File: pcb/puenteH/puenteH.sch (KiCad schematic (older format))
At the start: 16 parts

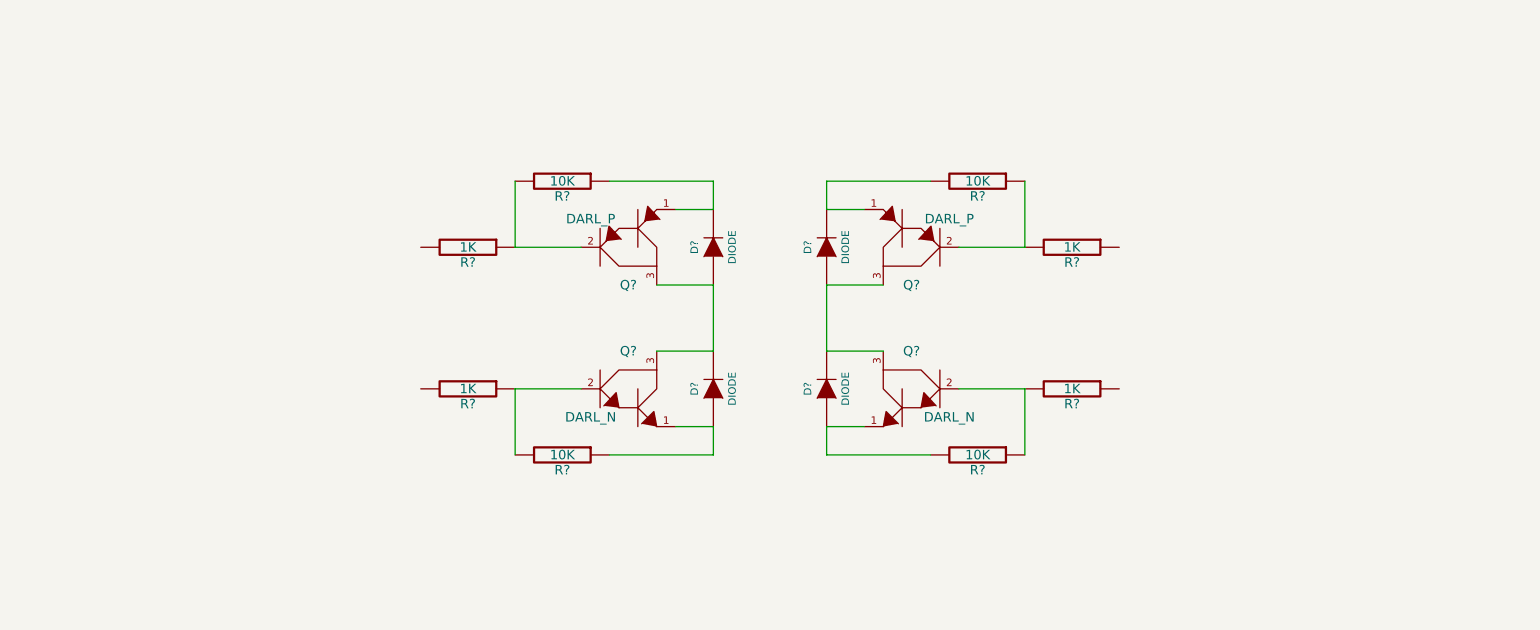
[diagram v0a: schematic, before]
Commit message: Add optos for digital signals
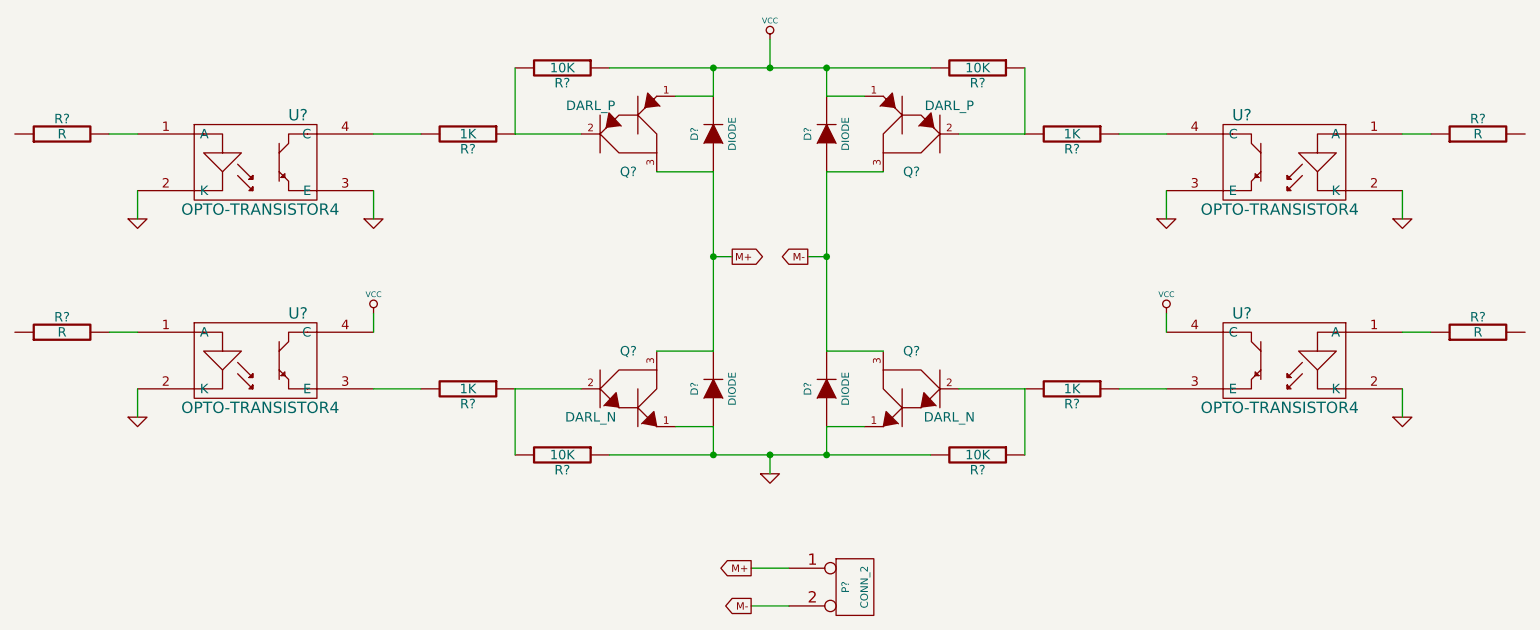
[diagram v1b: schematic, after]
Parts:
- added P?: CONN_2, symbol CONN_2
- added R? (x4): R, symbol R
- added U? (x4): OPTO-TRANSISTOR4, symbol OPTO-TRANSISTOR4
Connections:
- net M+: now reaches D?.1 (A), D?.2 (K), Q?.3, Q?.3
- net M+: now also P?.1 (P1)
- net VCC: now reaches D?.2 (K), Q?.1, R?.1
- net VCC: now also D?.2 (K), Q?.1, R?.2, U?.4 (C), U?.4 (C)
- net M-: now reaches D?.1 (A), D?.2 (K), Q?.3, Q?.3
- net M-: now also P?.2 (PM)
- net GND: now reaches D?.1 (A), Q?.1, R?.2
- net GND: now also D?.1 (A), Q?.1, R?.1, U?.2 (K), U?.2 (K), U?.2 (K), U?.2 (K), U?.3 (E), U?.3 (E)
- net at R?.2: now also U?.3 (E)
- net at R?.2: now also U?.4 (C)
- net at R?.1: now also U?.4 (C)
- net at R?.1: now also U?.3 (E)
- new net: R?.2, U?.1 (A) (x2)
- new net: R?.1, U?.1 (A) (x2)
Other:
- moved on the sheet: D?, Q?, R?

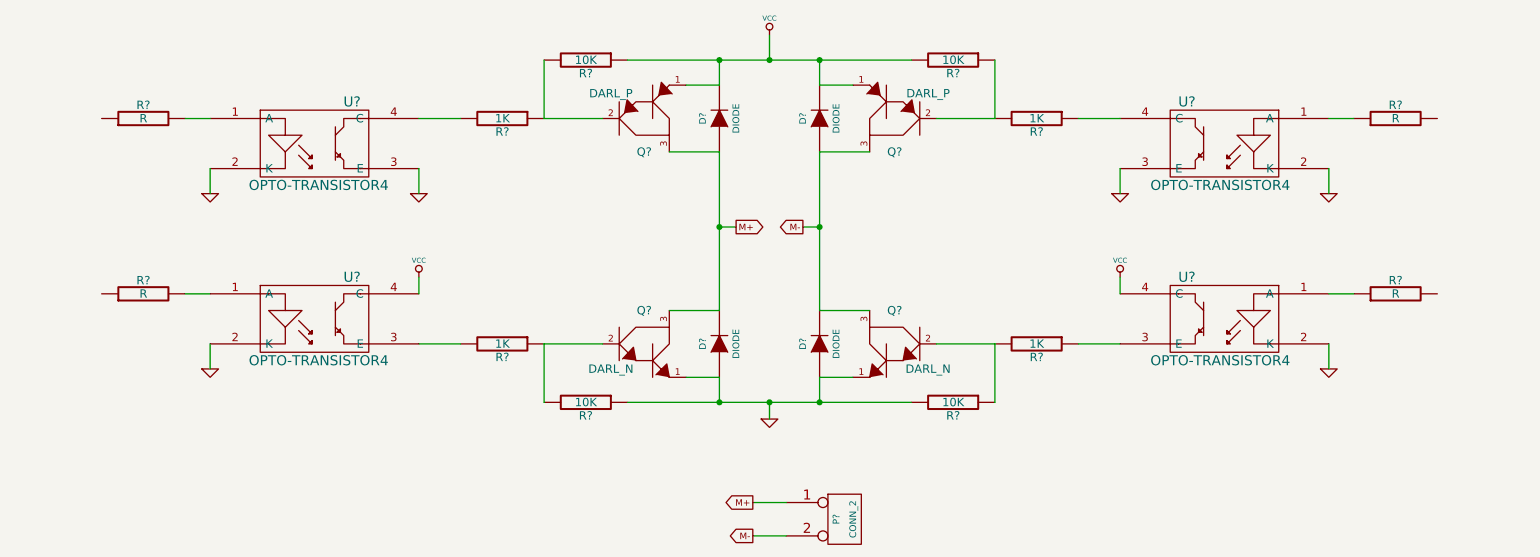
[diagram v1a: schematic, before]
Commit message: Add pins for interface between the H bridge and the uC
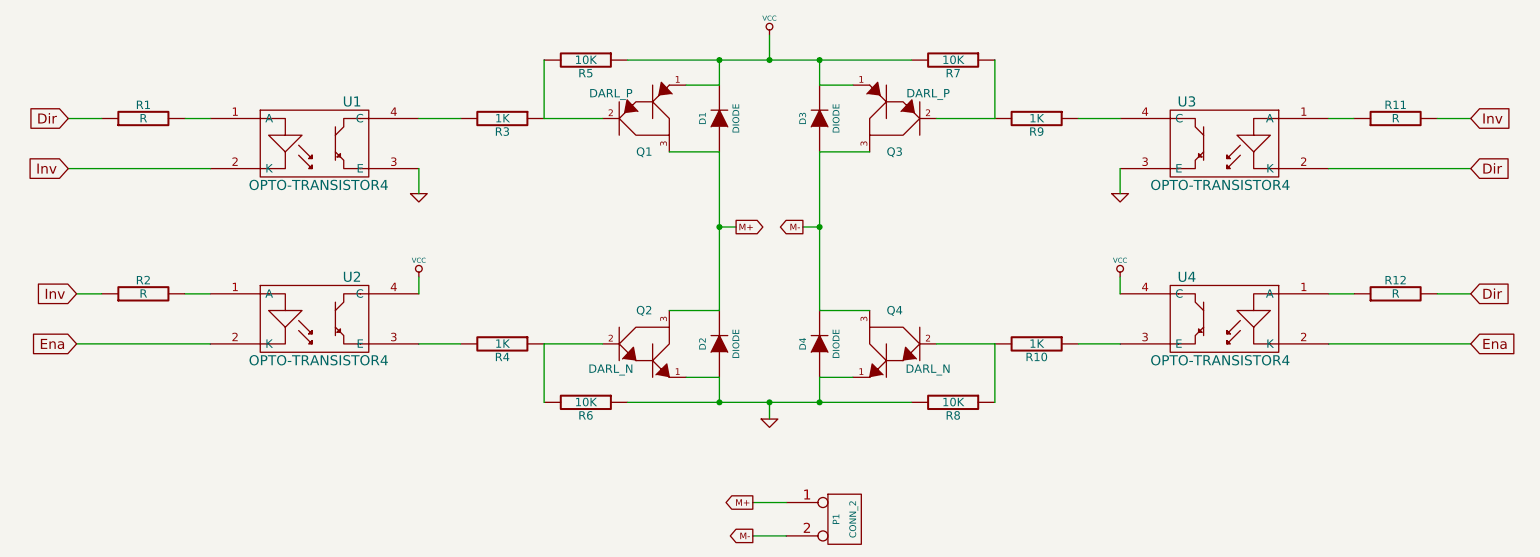
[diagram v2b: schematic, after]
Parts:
- gave numbers to parts that had none: 25
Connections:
- net GND: no longer U1.2 (K), U2.2 (K), U3.2 (K), U4.2 (K)
- net Inv: now reaches R2.1
- net Inv: now also R11.2, U1.2 (K)
- net Dir: now reaches R1.1
- net Dir: now also R12.2, U3.2 (K)
- new net Ena: U2.2 (K), U4.2 (K)
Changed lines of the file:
@@
-EESchema Schematic File Version 2  date mar 11 dic 2012 20:15:30 UYST
+EESchema Schematic File Version 2  date vie 14 dic 2012 20:56:03 UYST
 LIBS:power
 LIBS:device
@@
 Sheet 1 1
 Title "Puente H para motores CC"
-Date "11 dec 2012"
+Date "14 dec 2012"
 Rev "1.0"
 Comp ""
@@
 $EndDescr
 Wire Wire Line
+	9600 3100 9800 3100
+Wire Wire Line
+	1450 4150 1600 4150
+Wire Wire Line
+	9800 4150 9600 4150
+Wire Wire Line
+	1400 3400 2250 3400
+Wire Wire Line
 	7700 4050 7700 4150
 Wire Wire Line
@@
 Wire Wire Line
 	8950 3100 9100 3100
-Wire Wire Line
-	8950 3400 8950 3550
-Wire Wire Line
-	2250 4450 2250 4600
-Wire Wire Line
-	2250 3400 2250 3550
 Wire Wire Line
 	3500 3100 3750 3100
@@
 	2100 4150 2250 4150
 Wire Wire Line
-	8950 4450 8950 4600
-Wire Wire Line
 	8950 4150 9100 4150
 Wire Wire Line
@@
 Wire Wire Line
 	7700 3400 7700 3550
-$Comp
-L VCC #PWR?
+Wire Wire Line
+	1400 3100 1600 3100
+Wire Wire Line
+	2250 4450 1450 4450
+Wire Wire Line
+	9800 4450 8950 4450
+Wire Wire Line
+	8950 3400 9800 3400
+Text GLabel 9800 3400 2    60   Input ~ 0
+Dir
+Text GLabel 1450 4150 0    60   Input ~ 0
+Inv
+Text GLabel 9800 4450 2    60   Input ~ 0
+Ena
+Text GLabel 9800 3100 2    60   Input ~ 0
+Inv
+Text GLabel 9800 4150 2    60   Input ~ 0
+Dir
+Text GLabel 1450 4450 0    60   Input ~ 0
+Ena
+Text GLabel 1400 3400 0    60   Input ~ 0
+Inv
+Text GLabel 1400 3100 0    60   Input ~ 0
+Dir
+$Comp
+L VCC #PWR6
 U 1 1 50C7B069
 P 7700 4050
-F 0 "#PWR?" H 7700 4150 30  0001 C CNN
+F 0 "#PWR6" H 7700 4150 30  0001 C CNN
 F 1 "VCC" H 7700 4150 30  0000 C CNN
 	1    7700 4050
@@
 $EndComp
 $Comp
-L GND #PWR?
+L GND #PWR5
 U 1 1 50C7B05F
 P 7700 3550
-F 0 "#PWR?" H 7700 3550 30  0001 C CNN
+F 0 "#PWR5" H 7700 3550 30  0001 C CNN
 F 1 "GND" H 7700 3480 30  0001 C CNN
 	1    7700 3550
@@
 $EndComp
 $Comp
-L VCC #PWR?
+L VCC #PWR2
 U 1 1 50C7B04C
 P 3500 4050
-F 0 "#PWR?" H 3500 4150 30  0001 C CNN
+F 0 "#PWR2" H 3500 4150 30  0001 C CNN
 F 1 "VCC" H 3500 4150 30  0000 C CNN
 	1    3500 4050
@@
 $EndComp
 $Comp
-L GND #PWR?
+L GND #PWR1
 U 1 1 50C7B034
 P 3500 3550
-F 0 "#PWR?" H 3500 3550 30  0001 C CNN
+F 0 "#PWR1" H 3500 3550 30  0001 C CNN
 F 1 "GND" H 3500 3480 30  0001 C CNN
 	1    3500 3550
@@
 $EndComp
 $Comp
-L R R?
+L R R12
 U 1 1 50C7AECB
 P 9350 4150
-F 0 "R?" V 9430 4150 50  0000 C CNN
+F 0 "R12" V 9430 4150 50  0000 C CNN
 F 1 "R" V 9350 4150 50  0000 C CNN
 	1    9350 4150
@@
 $EndComp
 $Comp
-L R R?
+L R R11
 U 1 1 50C7AEBA
 P 9350 3100
-F 0 "R?" V 9430 3100 50  0000 C CNN
+F 0 "R11" V 9430 3100 50  0000 C CNN
 F 1 "R" V 9350 3100 50  0000 C CNN
 	1    9350 3100
@@
 $EndComp
 $Comp
-L GND #PWR?
-U 1 1 50C7AEAD
-P 8950 3550
-F 0 "#PWR?" H 8950 3550 30  0001 C CNN
-F 1 "GND" H 8950 3480 30  0001 C CNN
-	1    8950 3550
-	1    0    0    -1
-$EndComp
-$Comp
-L GND #PWR?
-U 1 1 50C7AE9A
-P 8950 4600
-F 0 "#PWR?" H 8950 4600 30  0001 C CNN
-F 1 "GND" H 8950 4530 30  0001 C CNN
-	1    8950 4600
-	1    0    0    -1
-$EndComp
-$Comp
-L R R?
+L R R1
 U 1 1 50C7A976
 P 1850 3100
-F 0 "R?" V 1930 3100 50  0000 C CNN
+F 0 "R1" V 1930 3100 50  0000 C CNN
 F 1 "R" V 1850 3100 50  0000 C CNN
 	1    1850 3100
@@
 $EndComp
 $Comp
-L GND #PWR?
-U 1 1 50C7A970
-P 2250 3550
-F 0 "#PWR?" H 2250 3550 30  0001 C CNN
-F 1 "GND" H 2250 3480 30  0001 C CNN
-	1    2250 3550
-	1    0    0    -1
-$EndComp
-$Comp
-L GND #PWR?
-U 1 1 50C7A961
-P 2250 4600
-F 0 "#PWR?" H 2250 4600 30  0001 C CNN
-F 1 "GND" H 2250 4530 30  0001 C CNN
-	1    2250 4600
-	1    0    0    -1
-$EndComp
-$Comp
-L R R?
+L R R2
 U 1 1 50C7A94E
 P 1850 4150
-F 0 "R?" V 1930 4150 50  0000 C CNN
+F 0 "R2" V 1930 4150 50  0000 C CNN
 F 1 "R" V 1850 4150 50  0000 C CNN
 	1    1850 4150
@@
 $EndComp
 $Comp
-L OPTO-TRANSISTOR4 U?
+L OPTO-TRANSISTOR4 U3
 U 1 1 50C7A839
 P 8300 3250
-F 0 "U?" H 8500 3500 60  0000 C CNN
+F 0 "U3" H 8500 3500 60  0000 C CNN
 F 1 "OPTO-TRANSISTOR4" H 8300 3000 60  0000 C CNN
 	1    8300 3250
@@
 $EndComp
 $Comp
-L OPTO-TRANSISTOR4 U?
+L OPTO-TRANSISTOR4 U1
 U 1 1 50C7A810
 P 2900 3250
-F 0 "U?" H 3100 3500 60  0000 C CNN
+F 0 "U1" H 3100 3500 60  0000 C CNN
 F 1 "OPTO-TRANSISTOR4" H 2900 3000 60  0000 C CNN
 	1    2900 3250
@@
 M+
 $Comp
-L CONN_2 P?
+L CONN_2 P1
 U 1 1 50C7A575
 P 6050 5500
-F 0 "P?" V 6000 5500 40  0000 C CNN
+F 0 "P1" V 6000 5500 40  0000 C CNN
 F 1 "CONN_2" V 6100 5500 40  0000 C CNN
 	1    6050 5500
@@
 M-
 $Comp
-L OPTO-TRANSISTOR4 U?
+L OPTO-TRANSISTOR4 U4
 U 1 1 50C79F62
 P 8300 4300
-F 0 "U?" H 8500 4550 60  0000 C CNN
+F 0 "U4" H 8500 4550 60  0000 C CNN
 F 1 "OPTO-TRANSISTOR4" H 8300 4050 60  0000 C CNN
 	1    8300 4300
@@
 $EndComp
 $Comp
-L OPTO-TRANSISTOR4 U?
+L OPTO-TRANSISTOR4 U2
 U 1 1 50C79F19
 P 2900 4300
-F 0 "U?" H 3100 4550 60  0000 C CNN
+F 0 "U2" H 3100 4550 60  0000 C CNN
 F 1 "OPTO-TRANSISTOR4" H 2900 4050 60  0000 C CNN
 	1    2900 4300
@@
 $EndComp
 $Comp
-L GND #PWR01
+L GND #PWR4
 U 1 1 50C79DFE
 P 5600 4900
-F 0 "#PWR01" H 5600 4900 30  0001 C CNN
+F 0 "#PWR4" H 5600 4900 30  0001 C CNN
 F 1 "GND" H 5600 4830 30  0001 C CNN
 	1    5600 4900
@@
 $EndComp
 $Comp
-L VCC #PWR02
+L VCC #PWR3
 U 1 1 50C79CA1
 P 5600 2600
-F 0 "#PWR02" H 5600 2700 30  0001 C CNN
+F 0 "#PWR3" H 5600 2700 30  0001 C CNN
 F 1 "VCC" H 5600 2700 30  0000 C CNN
 	1    5600 2600
@@
 $EndComp
 $Comp
-L R R?
+L R R6
 U 1 1 50B6917D
 P 4500 4800
-F 0 "R?" V 4580 4800 50  0000 C CNN
+F 0 "R6" V 4580 4800 50  0000 C CNN
 F 1 "10K" V 4500 4800 50  0000 C CNN
 	1    4500 4800
@@
 $EndComp
 $Comp
-L R R?
+L R R5
 U 1 1 50B69176
 P 4500 2750
-F 0 "R?" V 4580 2750 50  0000 C CNN
+F 0 "R5" V 4580 2750 50  0000 C CNN
 F 1 "10K" V 4500 2750 50  0000 C CNN
 	1    4500 2750
@@
 $EndComp
 $Comp
-L R R?
+L R R8
 U 1 1 50B6915C
 P 6700 4800
-F 0 "R?" V 6780 4800 50  0000 C CNN
+F 0 "R8" V 6780 4800 50  0000 C CNN
 F 1 "10K" V 6700 4800 50  0000 C CNN
 	1    6700 4800
@@
 $EndComp
 $Comp
-L R R?
+L R R7
 U 1 1 50B69138
 P 6700 2750
-F 0 "R?" V 6780 2750 50  0000 C CNN
+F 0 "R7" V 6780 2750 50  0000 C CNN
 F 1 "10K" V 6700 2750 50  0000 C CNN
 	1    6700 2750
@@
 $EndComp
 $Comp
-L R R?
+L R R10
 U 1 1 50B6908A
 P 7200 4450
-F 0 "R?" V 7280 4450 50  0000 C CNN
+F 0 "R10" V 7280 4450 50  0000 C CNN
 F 1 "1K" V 7200 4450 50  0000 C CNN
 	1    7200 4450
@@
 $EndComp
 $Comp
-L R R?
+L R R9
 U 1 1 50B69089
 P 7200 3100
-F 0 "R?" V 7280 3100 50  0000 C CNN
+F 0 "R9" V 7280 3100 50  0000 C CNN
 F 1 "1K" V 7200 3100 50  0000 C CNN
 	1    7200 3100
@@
 $EndComp
 $Comp
-L R R?
+L R R3
 U 1 1 50B69053
 P 4000 3100
-F 0 "R?" V 4080 3100 50  0000 C CNN
+F 0 "R3" V 4080 3100 50  0000 C CNN
 F 1 "1K" V 4000 3100 50  0000 C CNN
 	1    4000 3100
@@
 $EndComp
 $Comp
-L R R?
+L R R4
 U 1 1 50B69034
 P 4000 4450
-F 0 "R?" V 4080 4450 50  0000 C CNN
+F 0 "R4" V 4080 4450 50  0000 C CNN
 F 1 "1K" V 4000 4450 50  0000 C CNN
 	1    4000 4450
@@
 $EndComp
 $Comp
-L DARL_P Q?
+L DARL_P Q3
 U 1 1 50B68FD6
 P 6350 3050
-F 0 "Q?" H 6350 3300 50  0000 C CNN
+F 0 "Q3" H 6350 3300 50  0000 C CNN
 F 1 "DARL_P" H 6150 2950 50  0000 C CNN
 	1    6350 3050
@@
 $EndComp
 $Comp
-L DARL_P Q?
+L DARL_P Q1
 U 1 1 50B68FBD
 P 4850 3050
-F 0 "Q?" H 4850 3300 50  0000 C CNN
+F 0 "Q1" H 4850 3300 50  0000 C CNN
 F 1 "DARL_P" H 4650 2950 50  0000 C CNN
 	1    4850 3050
@@
 $EndComp
 $Comp
-L DARL_N Q?
+L DARL_N Q4
 U 1 1 50B68A06
 P 6350 4500
-F 0 "Q?" H 6350 4750 50  0000 C CNN
+F 0 "Q4" H 6350 4750 50  0000 C CNN
 F 1 "DARL_N" H 6150 4400 50  0000 C CNN
 	1    6350 4500
@@
 $EndComp
 $Comp
-L DARL_N Q?
+L DARL_N Q2
 U 1 1 50B689ED
 P 4850 4500
-F 0 "Q?" H 4850 4750 50  0000 C CNN
+F 0 "Q2" H 4850 4750 50  0000 C CNN
 F 1 "DARL_N" H 4650 4400 50  0000 C CNN
 	1    4850 4500
@@
 $EndComp
 $Comp
-L DIODE D?
+L DIODE D2
 U 1 1 50B53F36
 P 5300 4450
-F 0 "D?" H 5300 4550 40  0000 C CNN
+F 0 "D2" H 5300 4550 40  0000 C CNN
 F 1 "DIODE" H 5300 4350 40  0000 C CNN
 	1    5300 4450
@@
 $EndComp
 $Comp
-L DIODE D?
+L DIODE D4
 U 1 1 50B53F35
 P 5900 4450
-F 0 "D?" H 5900 4550 40  0000 C CNN
+F 0 "D4" H 5900 4550 40  0000 C CNN
 F 1 "DIODE" H 5900 4350 40  0000 C CNN
 	1    5900 4450
@@
 $EndComp
 $Comp
-L DIODE D?
+L DIODE D3
 U 1 1 50B53F1B
 P 5900 3100
-F 0 "D?" H 5900 3200 40  0000 C CNN
+F 0 "D3" H 5900 3200 40  0000 C CNN
 F 1 "DIODE" H 5900 3000 40  0000 C CNN
 	1    5900 3100
@@
 $EndComp
 $Comp
-L DIODE D?
+L DIODE D1
 U 1 1 50B53F09
 P 5300 3100
-F 0 "D?" H 5300 3200 40  0000 C CNN
+F 0 "D1" H 5300 3200 40  0000 C CNN
 F 1 "DIODE" H 5300 3000 40  0000 C CNN
 	1    5300 3100

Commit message: Add table of true
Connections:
- net Ena renamed En
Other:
- note added: "Dir"
- note added: "En"
- note added: "Inv"
- note added: "Movimiento"
- note added: "Tabla de verdad"
- moved on the sheet: D1, D2, D3, D4, P1, Q1, Q2, Q3, Q4, R1, R10, R11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
